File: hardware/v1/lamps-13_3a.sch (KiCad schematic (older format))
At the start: 11 parts, among them P1 CONN_02X05, P2 CONN_01X04, P3 CONN_01X04

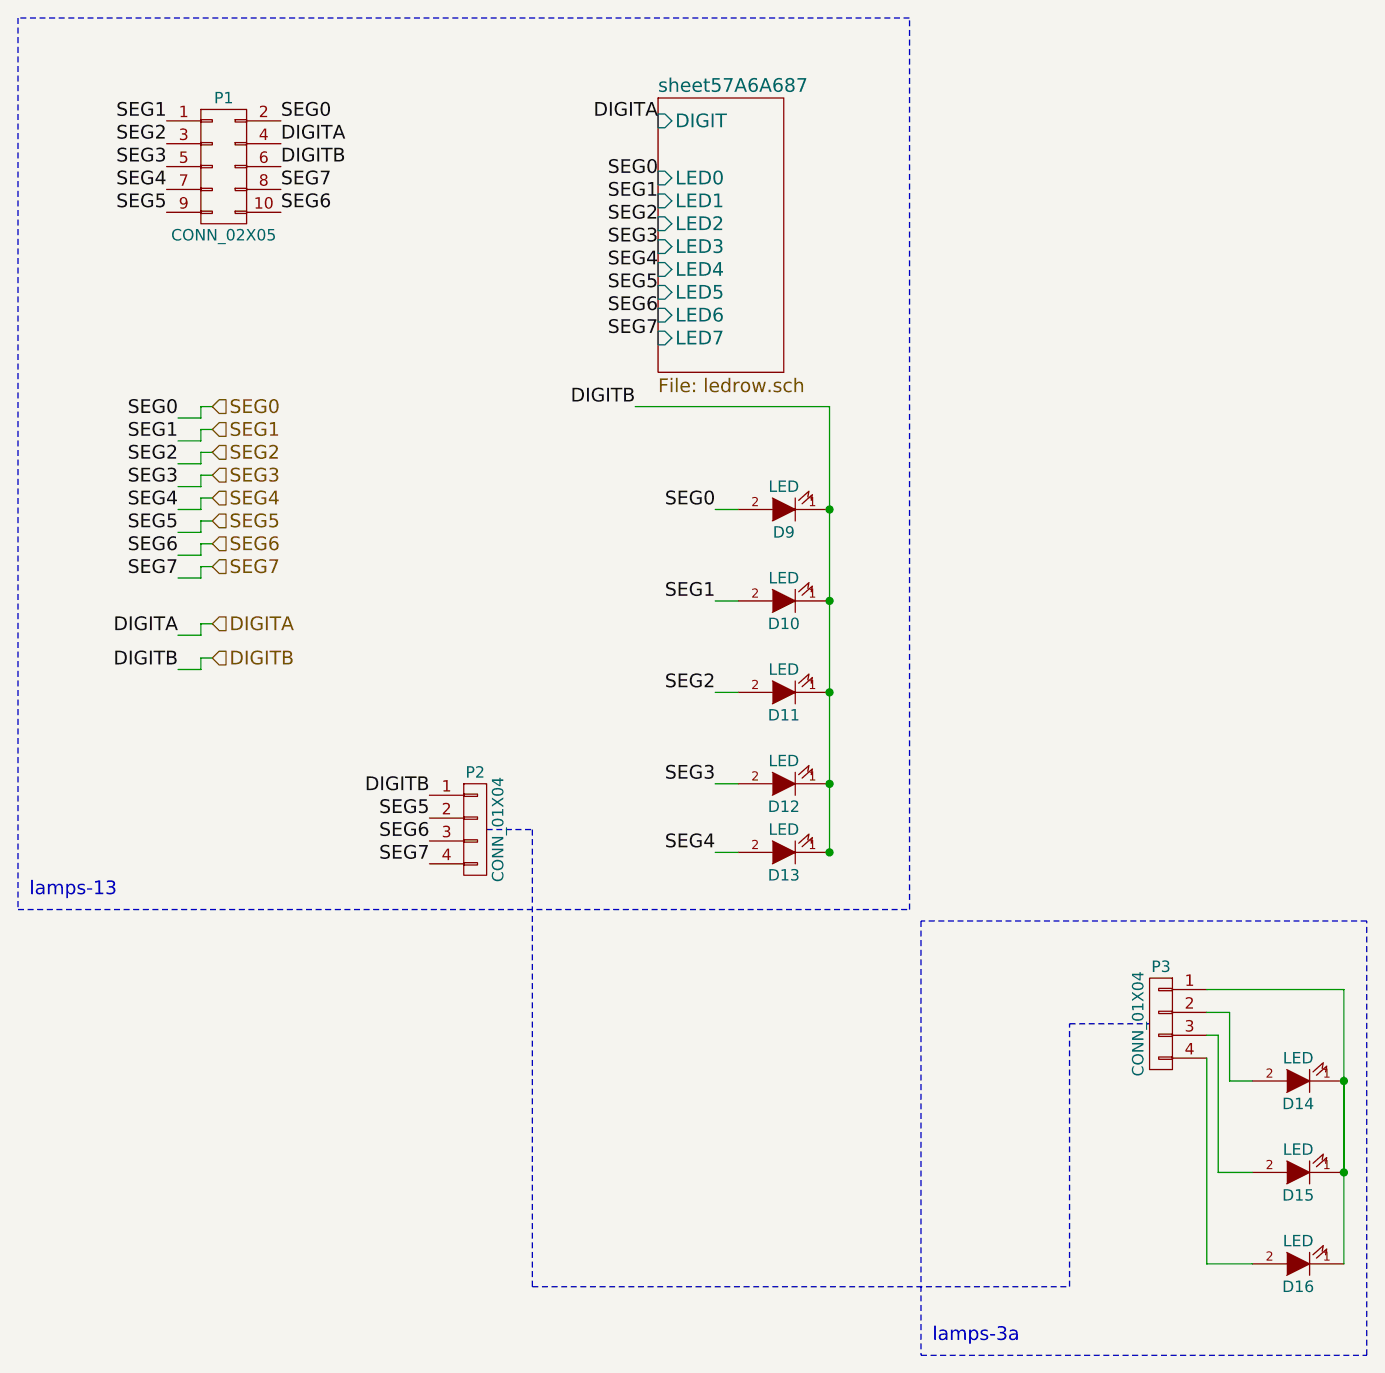
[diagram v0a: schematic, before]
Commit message: Add new schematics for additional switch boards
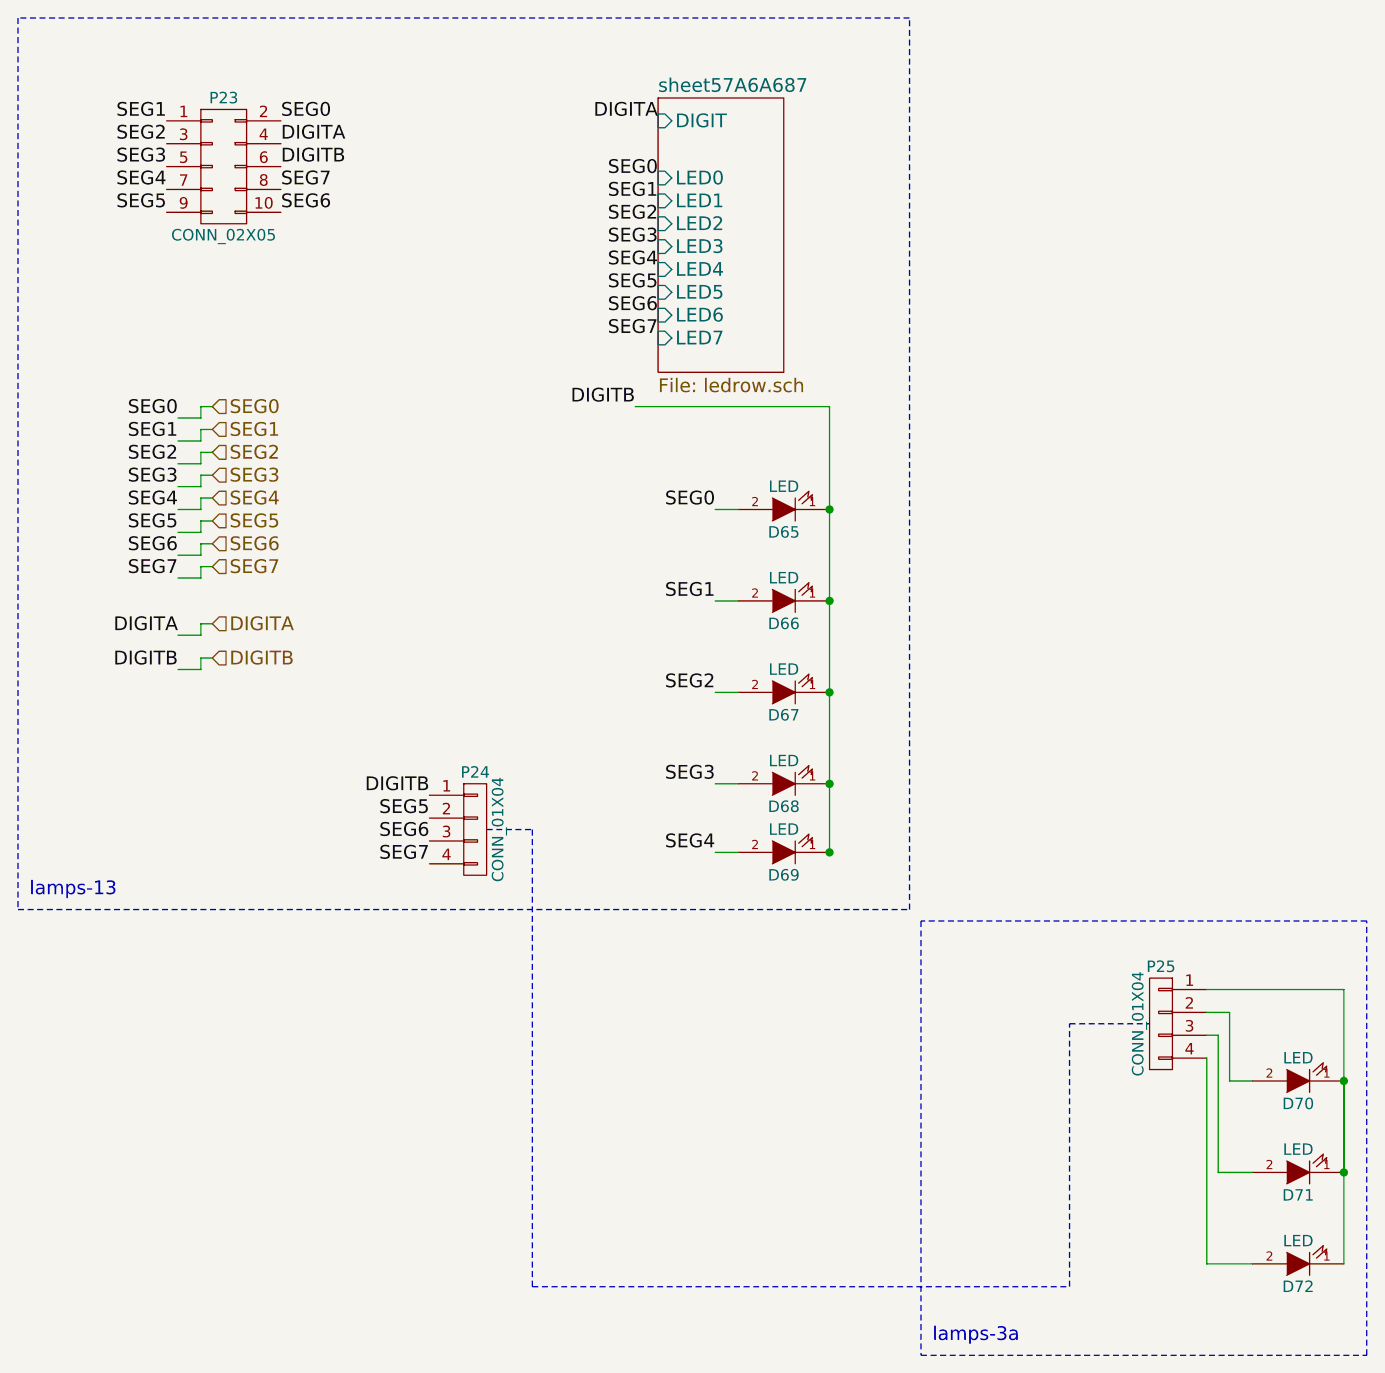
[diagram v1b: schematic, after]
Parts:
- P23: renamed from P1; footprint Pin_Headers:Pin_Header_Angled_2x05 -> Pin_Headers:Pin_Header_Straight_2x05
- renumbered D9 to D65, D10 to D66, D11 to D67, D12 to D68, D13 to D69, D14 to D70, D15 to D71, D16 to D72, P2 to P24, P3 to P25
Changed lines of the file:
@@
 $Descr A4 11693 8268
 encoding utf-8
-Sheet 1 27
+Sheet 1 30
 Title ""
 Date ""
@@
 $EndSheet
 $Comp
-L CONN_02X05 P1
+L CONN_02X05 P23
 U 1 1 57A6A6DA
 P 2000 1450
-F 0 "P1" H 2000 1750 50  0000 C CNN
+F 0 "P23" H 2000 1750 50  0000 C CNN
 F 1 "CONN_02X05" H 2000 1150 50  0000 C CNN
-F 2 "Pin_Headers:Pin_Header_Angled_2x05" H 2000 250 50  0001 C CNN
+F 2 "Pin_Headers:Pin_Header_Straight_2x05" H 2000 250 50  0001 C CNN
 F 3 "" H 2000 250 50  0000 C CNN
 	1    2000 1450
@@
 DIGITB
 $Comp
-L LED D16
+L LED D72
 U 1 1 57A6B27B
 P 6700 6250
-F 0 "D16" H 6700 6350 50  0000 C CNN
+F 0 "D72" H 6700 6350 50  0000 C CNN
 F 1 "LED" H 6700 6150 50  0000 C CNN
 F 2 "myparts:LED-5MM-custom" H 6700 6250 50  0001 C CNN
@@
 $EndComp
 $Comp
-L LED D15
+L LED D71
 U 1 1 57A6B282
 P 6700 5850
-F 0 "D15" H 6700 5950 50  0000 C CNN
+F 0 "D71" H 6700 5950 50  0000 C CNN
 F 1 "LED" H 6700 5750 50  0000 C CNN
 F 2 "myparts:LED-5MM-custom" H 6700 5850 50  0001 C CNN
@@
 $EndComp
 $Comp
-L LED D14
+L LED D70
 U 1 1 57A6B289
 P 6700 5450
-F 0 "D14" H 6700 5550 50  0000 C CNN
+F 0 "D70" H 6700 5550 50  0000 C CNN
 F 1 "LED" H 6700 5350 50  0000 C CNN
 F 2 "myparts:LED-5MM-custom" H 6700 5450 50  0001 C CNN
@@
 $EndComp
 $Comp
-L LED D13
+L LED D69
 U 1 1 57A6B290
 P 4450 4450
-F 0 "D13" H 4450 4550 50  0000 C CNN
+F 0 "D69" H 4450 4550 50  0000 C CNN
 F 1 "LED" H 4450 4350 50  0000 C CNN
 F 2 "myparts:LED-5MM-custom" H 4450 4450 50  0001 C CNN
@@
 $EndComp
 $Comp
-L LED D12
+L LED D68
 U 1 1 57A6B297
 P 4450 4150
-F 0 "D12" H 4450 4250 50  0000 C CNN
+F 0 "D68" H 4450 4250 50  0000 C CNN
 F 1 "LED" H 4450 4050 50  0000 C CNN
 F 2 "myparts:LED-5MM-custom" H 4450 4150 50  0001 C CNN
@@
 $EndComp
 $Comp
-L LED D11
+L LED D67
 U 1 1 57A6B29E
 P 4450 3750
-F 0 "D11" H 4450 3850 50  0000 C CNN
+F 0 "D67" H 4450 3850 50  0000 C CNN
 F 1 "LED" H 4450 3650 50  0000 C CNN
 F 2 "myparts:LED-5MM-custom" H 4450 3750 50  0001 C CNN
@@
 $EndComp
 $Comp
-L LED D10
+L LED D66
 U 1 1 57A6B2A5
 P 4450 3350
-F 0 "D10" H 4450 3450 50  0000 C CNN
+F 0 "D66" H 4450 3450 50  0000 C CNN
 F 1 "LED" H 4450 3250 50  0000 C CNN
 F 2 "myparts:LED-5MM-custom" H 4450 3350 50  0001 C CNN
@@
 $EndComp
 $Comp
-L LED D9
+L LED D65
 U 1 1 57A6B2AC
 P 4450 2950
-F 0 "D9" H 4450 3050 50  0000 C CNN
+F 0 "D65" H 4450 3050 50  0000 C CNN
 F 1 "LED" H 4450 2850 50  0000 C CNN
 F 2 "myparts:LED-5MM-custom" H 4450 2950 50  0001 C CNN
@@
 Connection ~ 6900 5850
 $Comp
-L CONN_01X04 P2
+L CONN_01X04 P24
 U 1 1 57A6C5AD
 P 3100 4350
-F 0 "P2" H 3100 4600 50  0000 C CNN
+F 0 "P24" H 3100 4600 50  0000 C CNN
 F 1 "CONN_01X04" V 3200 4350 50  0000 C CNN
 F 2 "Pin_Headers:Pin_Header_Straight_1x04" H 3100 4350 50  0001 C CNN
@@
 $EndComp
 $Comp
-L CONN_01X04 P3
+L CONN_01X04 P25
 U 1 1 57A6C629
 P 6100 5200
-F 0 "P3" H 6100 5450 50  0000 C CNN
+F 0 "P25" H 6100 5450 50  0000 C CNN
 F 1 "CONN_01X04" V 6200 5200 50  0000 C CNN
 F 2 "Pin_Headers:Pin_Header_Straight_1x04" H 6100 5200 50  0001 C CNN
